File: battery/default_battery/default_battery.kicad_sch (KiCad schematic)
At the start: 14 parts

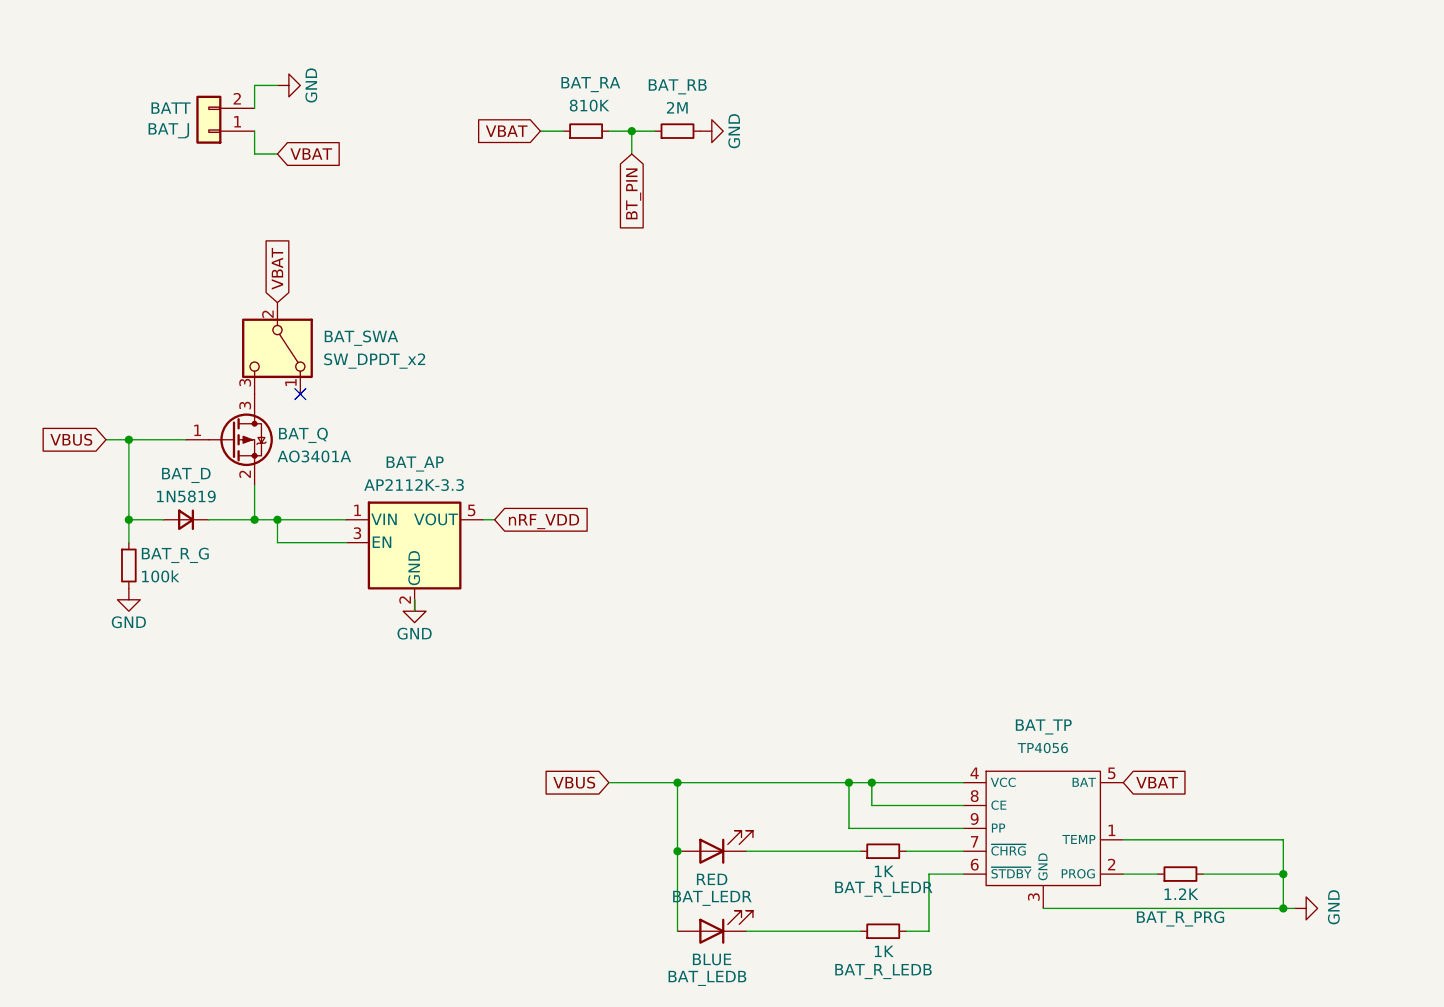
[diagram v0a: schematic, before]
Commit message: upgrade modules with kicad_sh and kicad_pcb
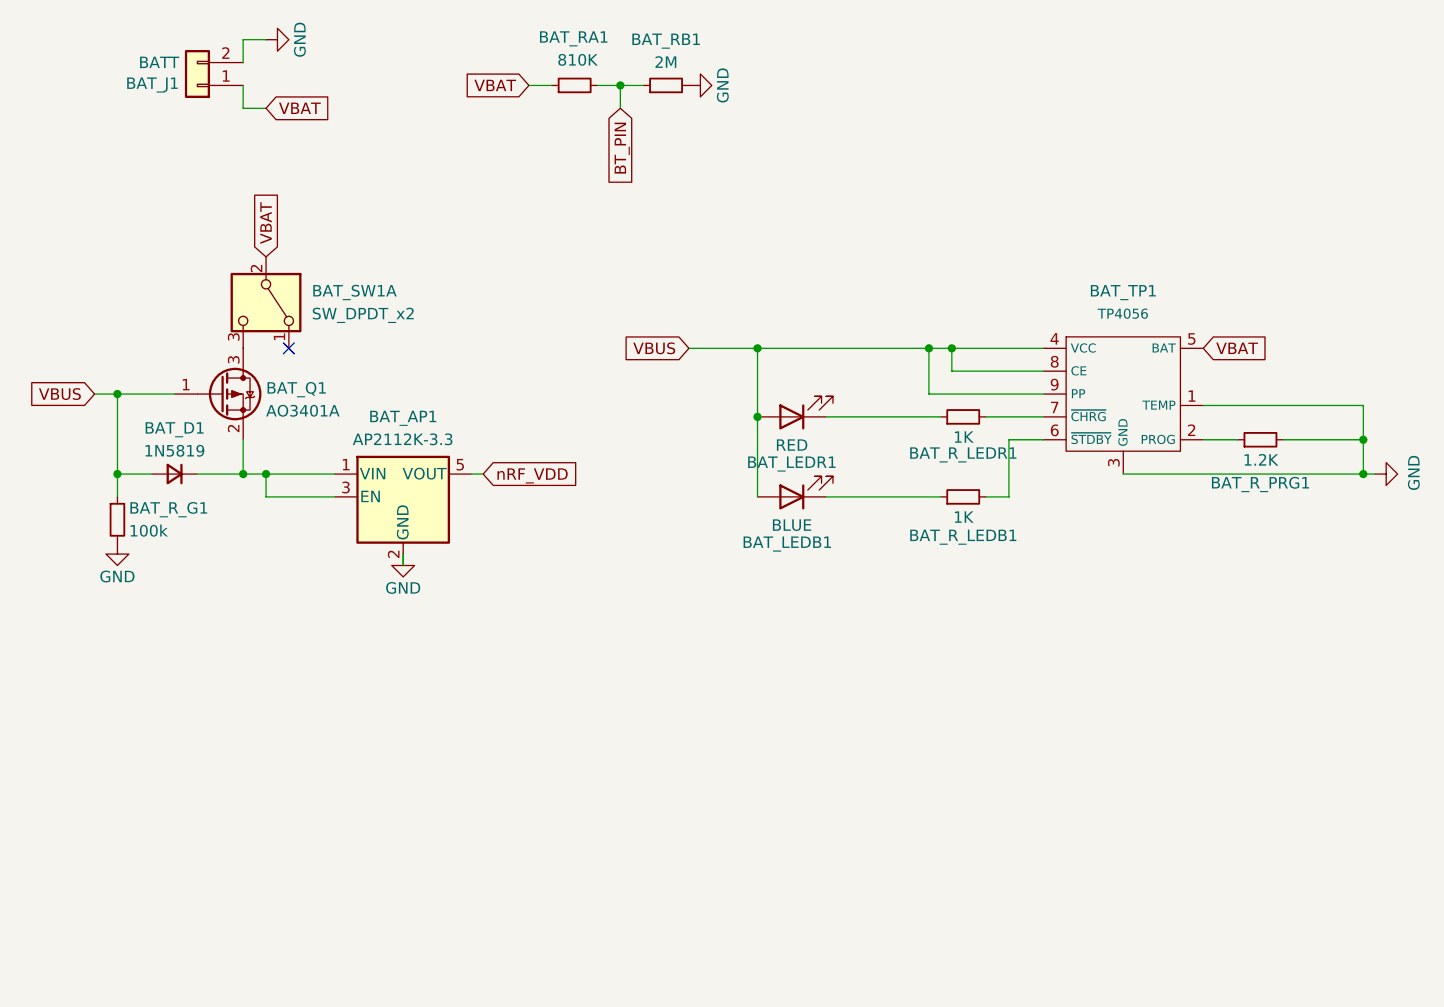
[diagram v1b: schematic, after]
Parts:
- renumbered BAT_AP to BAT_AP1, BAT_D to BAT_D1, BAT_J to BAT_J1, BAT_LEDB to BAT_LEDB1, BAT_LEDR to BAT_LEDR1, BAT_Q to BAT_Q1, BAT_RA to BAT_RA1, BAT_RB to BAT_RB1, BAT_R_G to BAT_R_G1, BAT_R_LEDB to BAT_R_LEDB1, BAT_R_LEDR to BAT_R_LEDR1, BAT_R_PRG to BAT_R_PRG1, BAT_SW to BAT_SW1, BAT_TP to BAT_TP1
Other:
- moved on the sheet: BAT_AP1, BAT_D1, BAT_J1, BAT_LEDB1, BAT_LEDR1, BAT_Q1, BAT_RA1, BAT_RB1, BAT_R_G1, BAT_R_LEDB1, BAT_R_LEDR1, BAT_R_PRG1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

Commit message: update battery module, change switch
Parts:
- BAT_SW1: footprint ErgoCai.pretty:MSK-12C02 -> ErgoCai.pretty:SK12D07VG4; symbol Switch:SW_DPDT_x2 -> ErgoCai:SK12D07VG4; Availability (none) -> Not in stock; Check_prices (none) -> https://www.snapeda.com/parts/SK12D07VG4/C%2526K/view-part/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; Description_1 (none) -> Switch Slide ON ON SPDT Side Slide 0.3A 30VDC PC Pins Brack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; MF (none) -> C&K; MP (none) -> SK12D07VG4; Package (none) -> None; Price (none) -> None; SnapEDA_Link (none) -> https://www.snapeda.com/parts/SK12D07VG4/C%2526K/view-part/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
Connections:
- net VBAT: now also BAT_SW1.COM; no longer BAT_SW1.2 (B)
- net at BAT_SW1.1: now also BAT_Q1.3 (D)
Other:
- moved on the sheet: BAT_SW1
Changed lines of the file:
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@@
 		(color 0 0 0 0)
 	)
+	(junction
+		(at 85.09 62.23)
+		(diameter 0)
+		(color 0 0 0 0)
+	)
 	(no_connect
-		(at 92.71 74.93)
+		(at 82.55 74.93)
 	)
 	(wire
@@
 	(wire
 		(pts
+			(xy 85.09 62.23) (xy 85.09 60.96)
+		)
+		(stroke
+			(width 0)
+			(type default)
+		)
+	)
+	(wire
+		(pts
 			(xy 119.38 45.72) (xy 121.92 45.72)
 		)
@@
 			(width 0)
 			(type solid)
+		)
+	)
+	(wire
+		(pts
+			(xy 85.09 63.5) (xy 85.09 62.23)
+		)
+		(stroke
+			(width 0)
+			(type default)
 		)
 	)
@@
 	(global_label "VBAT"
 		(shape input)
-		(at 90.17 64.77 90)
+		(at 85.09 60.96 90)
 		(fields_autoplaced yes)
 		(effects
@@
 		)
 		(property "Intersheetrefs" "${INTERSHEET_REFS}"
-			(at 90.17 57.37 90)
+			(at 85.09 53.56 90)
 			(effects
 				(font
@@
 	)
 	(symbol
-		(lib_id "Switch:SW_DPDT_x2")
-		(at 90.17 69.85 270)
+		(lib_id "ErgoCai:SK12D07VG4")
+		(at 85.09 67.31 180)
 		(unit 1)
 		(exclude_from_sim no)
@@
 		(fields_autoplaced yes)
 		(property "Reference" "BAT_SW1"
-			(at 95.25 68.5799 90)
-			(effects
-				(font
-					(size 1.27 1.27)
-				)
-				(justify left)
+			(at 91.44 67.3099 0)
+			(effects
+				(font
+					(size 1.27 1.27)
+				)
+				(justify right)
 			)
 		)
 		(property "Value" "SW_DPDT_x2"
-			(at 95.25 71.1199 90)
-			(effects
-				(font
-					(size 1.27 1.27)
-				)
-				(justify left)
-			)
-		)
-		(property "Footprint" "ErgoCai.pretty:MSK-12C02"
-			(at 90.17 69.85 0)
-			(effects
-				(font
-					(size 1.27 1.27)
-				)
+			(at 91.44 69.8499 0)
+			(effects
+				(font
+					(size 1.27 1.27)
+				)
+				(justify right)
+			)
+		)
+		(property "Footprint" "ErgoCai.pretty:SK12D07VG4"
+			(at 85.09 67.31 0)
+			(effects
+				(font
+					(size 1.27 1.27)
+				)
+				(justify bottom)
 				(hide yes)
 			)
 		)
 		(property "Datasheet" "~"
-			(at 90.17 69.85 0)
+			(at 85.09 67.31 0)
 			(effects
 				(font
@@
 		)
 		(property "Description" "Switch, dual pole double throw, separate symbols"
-			(at 90.17 69.85 0)
-			(effects
-				(font
-					(size 1.27 1.27)
-				)
-				(hide yes)
-			)
-		)
-		(pin "6"
-		)
-		(pin "4"
-		)
-		(pin "5"
-		)
-		(pin "3"
+			(at 85.09 67.31 0)
+			(effects
+				(font
+					(size 1.27 1.27)
+				)
+				(hide yes)
+			)
+		)
+		(property "MF" "C&K"
+			(at 85.09 67.31 0)
+			(effects
+				(font
+					(size 1.27 1.27)
+				)
+				(justify bottom)
+				(hide yes)
+			)
+		)
+		(property "Description_1" "Switch Slide ON ON SPDT Side Slide 0.3A 30VDC PC Pins Bracket Mount/Through Hole Bulk"
+			(at 85.09 67.31 0)
+			(effects
+				(font
+					(size 1.27 1.27)
+				)
+				(justify bottom)
+				(hide yes)
+			)
+		)
+		(property "Package" "None"
+			(at 85.09 67.31 0)
+			(effects
+				(font
+					(size 1.27 1.27)
+				)
+				(justify bottom)
+				(hide yes)
+			)
+		)
+		(property "Price" "None"
+			(at 85.09 67.31 0)
+			(effects
+				(font
+					(size 1.27 1.27)
+				)
+				(justify bottom)
+				(hide yes)
+			)
+		)
+		(property "SnapEDA_Link" "https://www.snapeda.com/parts/SK12D07VG4/C%2526K/view-part/?ref=snap"
+			(at 85.09 67.31 0)
+			(effects
+				(font
+					(size 1.27 1.27)
+				)
+				(justify bottom)
+				(hide yes)
+			)
+		)
+		(property "MP" "SK12D07VG4"
+			(at 85.09 67.31 0)
+			(effects
+				(font
+					(size 1.27 1.27)
+				)
+				(justify bottom)
+				(hide yes)
+			)
+		)
+		(property "Availability" "Not in stock"
+			(at 85.09 67.31 0)
+			(effects
+				(font
+					(size 1.27 1.27)
+				)
+				(justify bottom)
+				(hide yes)
+			)
+		)
+		(property "Check_prices" "https://www.snapeda.com/parts/SK12D07VG4/C%2526K/view-part/?ref=eda"
+			(at 85.09 67.31 0)
+			(effects
+				(font
+					(size 1.27 1.27)
+				)
+				(justify bottom)
+				(hide yes)
+			)
+		)
+		(pin "COM"
 		)
 		(pin "2"

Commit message: replace VDD-nRF to VCC
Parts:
- BAT_SW1: value SW_DPDT_x2 -> (none)
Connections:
- net BT_PIN renamed ADC_BT
- net nRF_VDD renamed VCC
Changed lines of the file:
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@@
 		)
 	)
-	(global_label "BT_PIN"
+	(global_label "ADC_BT"
 		(shape input)
 		(at 129.54 48.26 270)
@@
 		)
 		(property "Intersheetrefs" "${INTERSHEET_REFS}"
-			(at 129.54 57.6557 90)
+			(at 129.54 58.079 90)
 			(effects
 				(font
@@
 		)
 	)
-	(global_label "nRF_VDD"
+	(global_label "VCC"
 		(shape input)
 		(at 114.3 88.9 0)
@@
 		)
 		(property "Intersheetrefs" "${INTERSHEET_REFS}"
-			(at 125.389 88.9 0)
+			(at 120.9138 88.9 0)
 			(effects
 				(font
@@
 			)
 		)
-		(property "Value" "SW_DPDT_x2"
+		(property "Value" ""
 			(at 91.44 69.8499 0)
 			(effects

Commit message: update battery switch symbol
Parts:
- BAT_SW1: value (none) -> ~; footprint ErgoCai.pretty:SK12D07VG4 -> easyeda2kicad:SW-TH_SK12D07VG4; LCSC Part (none) -> C393937
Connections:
- net GND: now also BAT_SW1.4, BAT_SW1.5
- net VBAT: now also BAT_SW1.2; no longer BAT_SW1.COM
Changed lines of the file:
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@@
 	)
 	(junction
-		(at 85.09 62.23)
+		(at 80.01 63.5)
 		(diameter 0)
 		(color 0 0 0 0)
 	)
 	(no_connect
-		(at 82.55 74.93)
+		(at 80.01 58.42)
 	)
 	(wire
@@
 	(wire
 		(pts
-			(xy 85.09 62.23) (xy 85.09 60.96)
+			(xy 80.01 63.5) (xy 81.28 63.5)
 		)
 		(stroke
@@
 	(wire
 		(pts
-			(xy 85.09 63.5) (xy 85.09 62.23)
+			(xy 78.74 63.5) (xy 80.01 63.5)
+		)
+		(stroke
+			(width 0)
+			(type default)
+		)
+	)
+	(wire
+		(pts
+			(xy 87.63 68.58) (xy 87.63 74.93)
 		)
 		(stroke
@@
 		(pts
 			(xy 144.78 74.93) (xy 137.16 74.93)
+		)
+		(stroke
+			(width 0)
+			(type default)
+		)
+	)
+	(wire
+		(pts
+			(xy 80.01 68.58) (xy 87.63 68.58)
 		)
 		(stroke
@@
 	(global_label "VBAT"
 		(shape input)
-		(at 85.09 60.96 90)
+		(at 81.28 63.5 0)
 		(fields_autoplaced yes)
 		(effects
@@
 		)
 		(property "Intersheetrefs" "${INTERSHEET_REFS}"
-			(at 85.09 53.56 90)
+			(at 88.68 63.5 0)
 			(effects
 				(font
@@
 	(symbol
 		(lib_id "ErgoCai:SK12D07VG4")
-		(at 85.09 67.31 180)
+		(at 74.93 63.5 90)
 		(unit 1)
 		(exclude_from_sim no)
@@
 		(on_board yes)
 		(dnp no)
-		(fields_autoplaced yes)
 		(property "Reference" "BAT_SW1"
-			(at 91.44 67.3099 0)
+			(at 68.58 59.69 0)
 			(effects
 				(font
@@
 			)
 		)
-		(property "Value" ""
-			(at 91.44 69.8499 0)
+		(property "Value" "~"
+			(at 72.3901 69.85 0)
 			(effects
 				(font
@@
 			)
 		)
-		(property "Footprint" "ErgoCai.pretty:SK12D07VG4"
-			(at 85.09 67.31 0)
+		(property "Footprint" "easyeda2kicad:SW-TH_SK12D07VG4"
+			(at 74.93 63.5 0)
 			(effects
 				(font
@@
 			)
 		)
-		(property "Datasheet" "~"
-			(at 85.09 67.31 0)
+		(property "Datasheet" "https://lcsc.com/product-detail/Toggle-Switches_SHOU-HAN-SK12D07VG4_C393937.html"
+			(at 74.93 63.5 0)
 			(effects
 				(font
@@
 		)
 		(property "Description" "Switch, dual pole double throw, separate symbols"
-			(at 85.09 67.31 0)
+			(at 74.93 63.5 0)
 			(effects
 				(font
@@
 		)
 		(property "MF" "C&K"
-			(at 85.09 67.31 0)
+			(at 74.93 63.5 0)
 			(effects
 				(font
@@
 		)
 		(property "Description_1" "Switch Slide ON ON SPDT Side Slide 0.3A 30VDC PC Pins Bracket Mount/Through Hole Bulk"
-			(at 85.09 67.31 0)
+			(at 74.93 63.5 0)
 			(effects
 				(font
@@
 		)
 		(property "Package" "None"
-			(at 85.09 67.31 0)
+			(at 74.93 63.5 0)
 			(effects
 				(font
@@
 		)
 		(property "Price" "None"
-			(at 85.09 67.31 0)
+			(at 74.93 63.5 0)
 			(effects
 				(font
@@
 		)
 		(property "SnapEDA_Link" "https://www.snapeda.com/parts/SK12D07VG4/C%2526K/view-part/?ref=snap"
-			(at 85.09 67.31 0)
+			(at 74.93 63.5 0)
 			(effects
 				(font
@@
 		)
 		(property "MP" "SK12D07VG4"
-			(at 85.09 67.31 0)
+			(at 74.93 63.5 0)
 			(effects
 				(font
@@
 		)
 		(property "Availability" "Not in stock"
-			(at 85.09 67.31 0)
+			(at 74.93 63.5 0)
 			(effects
 				(font
@@
 		)
 		(property "Check_prices" "https://www.snapeda.com/parts/SK12D07VG4/C%2526K/view-part/?ref=eda"
-			(at 85.09 67.31 0)
+			(at 74.93 63.5 0)
 			(effects
 				(font
@@
 			)
 		)
-		(pin "COM"
+		(property "LCSC Part" "C393937"
+			(at 92.71 63.5 0)
+			(effects
+				(font
+					(size 1.27 1.27)
+				)
+				(hide yes)
+			)
+		)
+		(pin "3"
 		)
 		(pin "2"
 		)
 		(pin "1"
+		)
+		(pin "4"
+		)
+		(pin "5"
 		)
 		(instances
@@
 				(path "/5ac02cf2-291a-487e-b868-5e66ea14e5ba"
 					(reference "BAT_R_LEDB1")
+					(unit 1)
+				)
+			)
+		)
+	)
+	(symbol
+		(lib_id "power:GND")
+		(at 80.01 55.88 90)
+		(unit 1)
+		(exclude_from_sim no)
+		(in_bom yes)
+		(on_board yes)
+		(dnp no)
+		(fields_autoplaced yes)
+		(property "Reference" "#PWR01"
+			(at 86.36 55.88 0)
+			(effects
+				(font
+					(size 1.27 1.27)
+				)
+				(hide yes)
+			)
+		)
+		(property "Value" "GND"
+			(at 84.4042 55.753 0)
+			(effects
+				(font
+					(size 1.27 1.27)
+				)
+			)
+		)
+		(property "Footprint" ""
+			(at 80.01 55.88 0)
+			(effects
+				(font
+					(size 1.27 1.27)
+				)
+				(hide yes)
+			)
+		)
+		(property "Datasheet" ""
+			(at 80.01 55.88 0)
+			(effects
+				(font
+					(size 1.27 1.27)
+				)
+				(hide yes)
+			)
+		)
+		(property "Description" "Power symbol creates a global label with name \"GND\" , ground"
+			(at 80.01 55.88 0)
+			(effects
+				(font
+					(size 1.27 1.27)
+				)
+				(hide yes)
+			)
+		)
+		(pin "1"
+		)
+		(instances
+			(project "default_battery"
+				(path "/5ac02cf2-291a-487e-b868-5e66ea14e5ba"
+					(reference "#PWR01")
 					(unit 1)
 				)
@@
 					(unit 1)
 				)
+			)
+		)
+	)
+	(symbol
+		(lib_id "power:GND")
+		(at 80.01 71.12 90)
+		(unit 1)
+		(exclude_from_sim no)
+		(in_bom yes)
+		(on_board yes)
+		(dnp no)
+		(property "Reference" "#PWR02"
+			(at 86.36 71.12 0)
+			(effects
+				(font
+					(size 1.27 1.27)
+				)
+				(hide yes)
+			)
+		)
+		(property "Value" "GND"
+			(at 84.4042 70.993 0)
+			(effects
+				(font
+					(size 1.27 1.27)
+				)
+			)
+		)
+		(property "Footprint" ""
+			(at 80.01 71.12 0)
+			(effects
+				(font
+					(size 1.27 1.27)
+				)
+				(hide yes)
+			)
+		)
+		(property "Datasheet" ""
+			(at 80.01 71.12 0)
+			(effects
+				(font
+					(size 1.27 1.27)
+				)
+				(hide yes)
+			)
+		)
+		(property "Description" "Power symbol creates a global label with name \"GND\" , ground"
+			(at 80.01 71.12 0)
+			(effects
+				(font
+					(size 1.27 1.27)
+				)
+				(hide yes)
+			)
+		)
+		(pin "1"
+		)
+		(instances
+			(project "default_battery"
+				(path "/5ac02cf2-291a-487e-b868-5e66ea14e5ba"
+					(reference "#PWR02")
+					(unit 1)
+				)
